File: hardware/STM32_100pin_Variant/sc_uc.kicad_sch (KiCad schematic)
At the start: 28 parts, among them J6 , U10 STM32L4S7VITx, U11 ATA6561-GAQW-N, Y4 Crystal_GND24

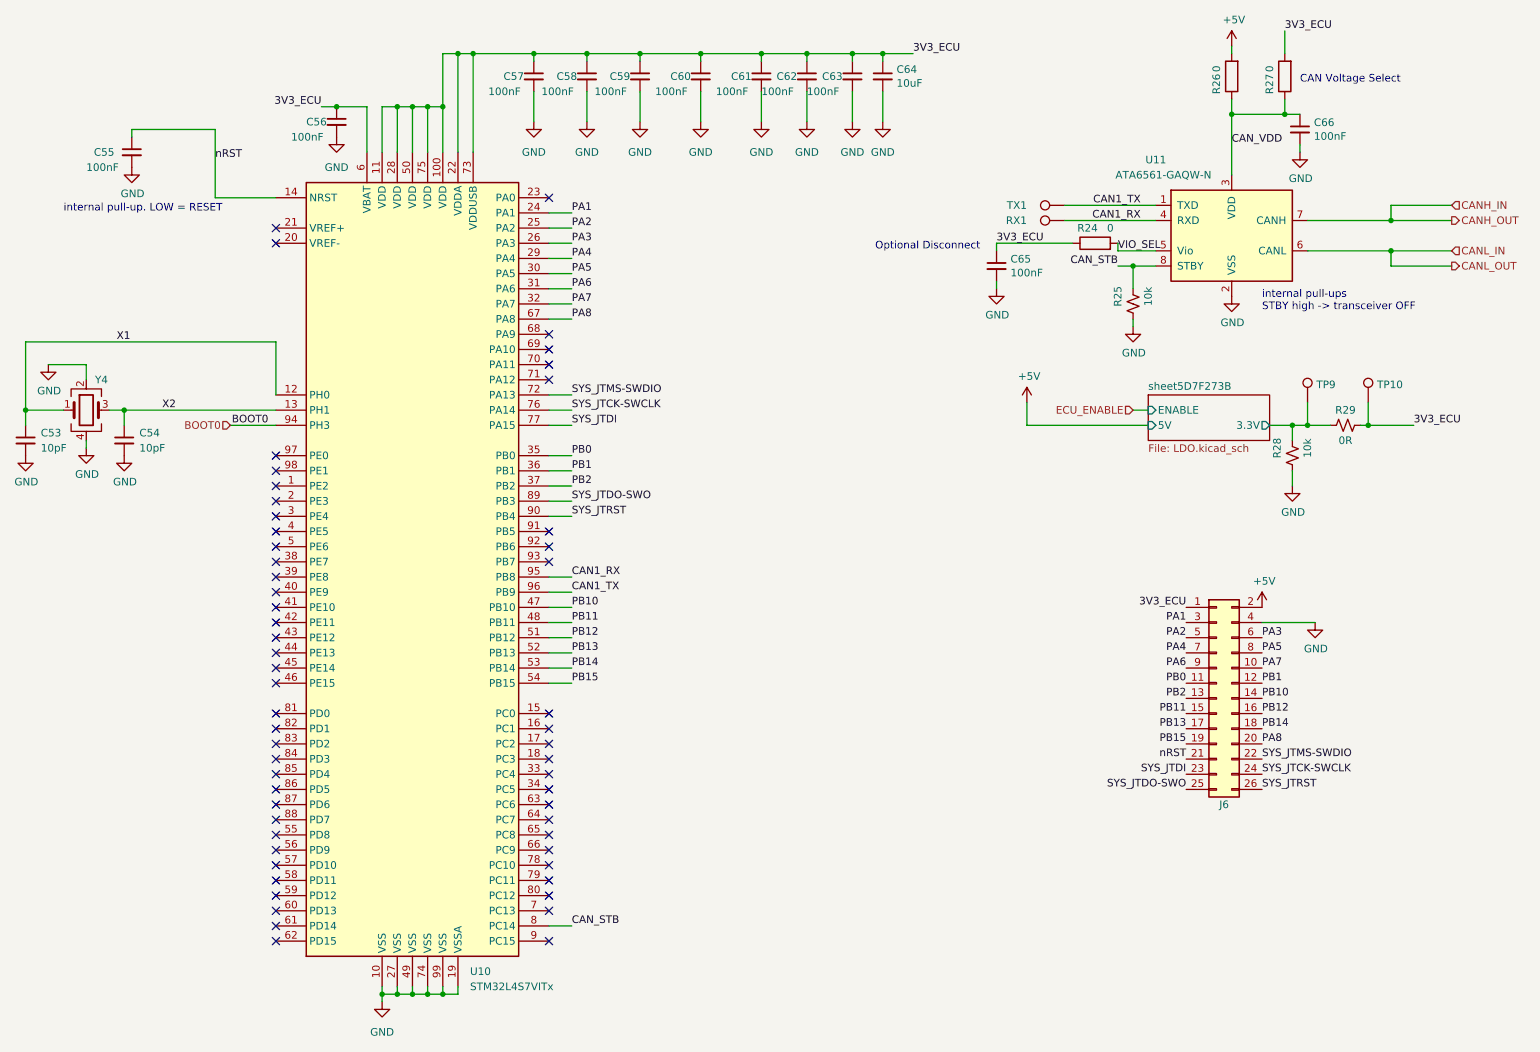
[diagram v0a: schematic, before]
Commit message: Schematic wiring fix, added part numbers
- Fixed missing connections between VREF+ and VDDA, VREF- and VSSA on all ECUs

- Added component part numbers for crystal and CAN trx to schematic
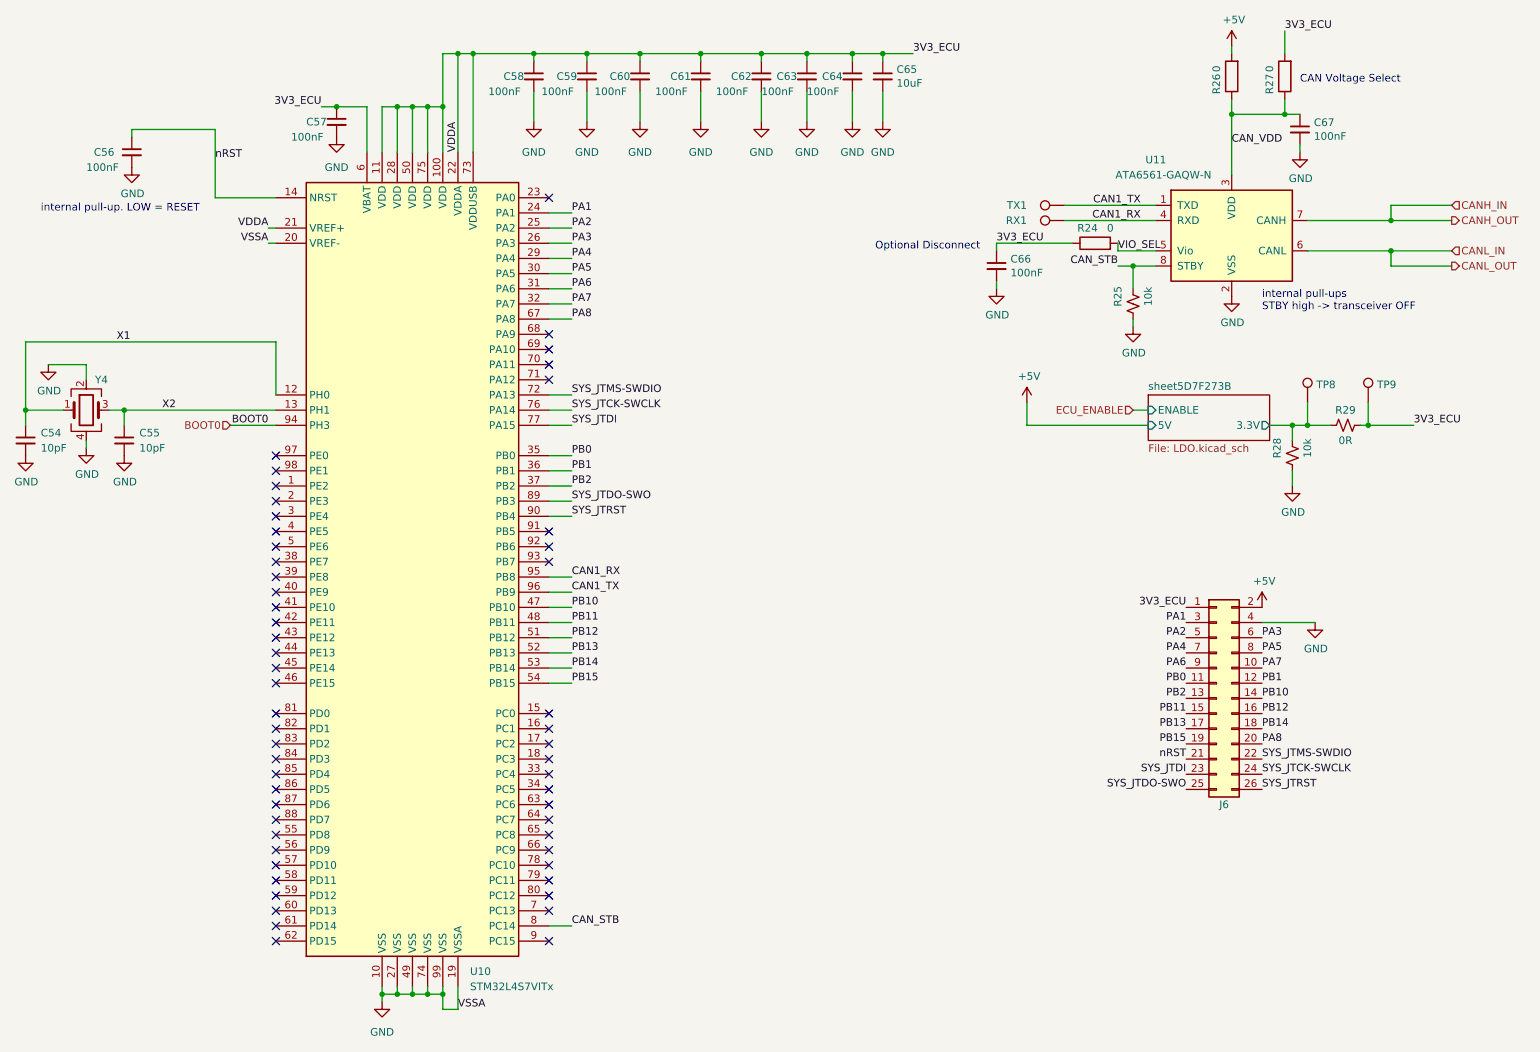
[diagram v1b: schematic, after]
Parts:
- U11: Part No.  (none) -> TCAN1042HGVDRQ1
- Y4: Part No. (none) -> CX3225GB10000D0HEQCC
- renumbered C53 to C54, C54 to C55, C55 to C56, C56 to C57, C57 to C58, C58 to C59, C59 to C60, C60 to C61, C61 to C62, C62 to C63, C63 to C64, C64 to C65, C65 to C66, C66 to C67, TP9 to TP8, TP10 to TP9
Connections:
- net 3V3_ECU: now also U10.21 (VREF+)
- net GND: now also U10.20 (VREF-)
- no-connect marks 57 -> 55

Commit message: Electrical Fix
- Fixed missing VREF+/- connections on ECUs

- Updated version number to V1.1

- Updated Gerbers

- Updated schematic PDF
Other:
- title: RAMN: Resistant Automotive Miniature Network V1.0 -> RAMN 100 Pin Variant
